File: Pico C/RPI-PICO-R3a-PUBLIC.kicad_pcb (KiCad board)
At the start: 2 copper layers, 53.7 x 21 mm, 53 parts, among them IC1 W25Q16JVUXIQ, J1 CON_PICO_40W_VER_C, J2 USB_C_Receptacle_USB2.0_16P, J3 SM03B-SRSS-TB, Q1 DMG1012T-7, U1 RP2040, U2 RT6150B-33GQW, Y1 ECS-120-8-33-JGN-TR

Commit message: Add files via upload
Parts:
- moved C16 0.71 mm to (135.0, 95.0)
- moved C17 0.28 mm to (136.2, 100.0)

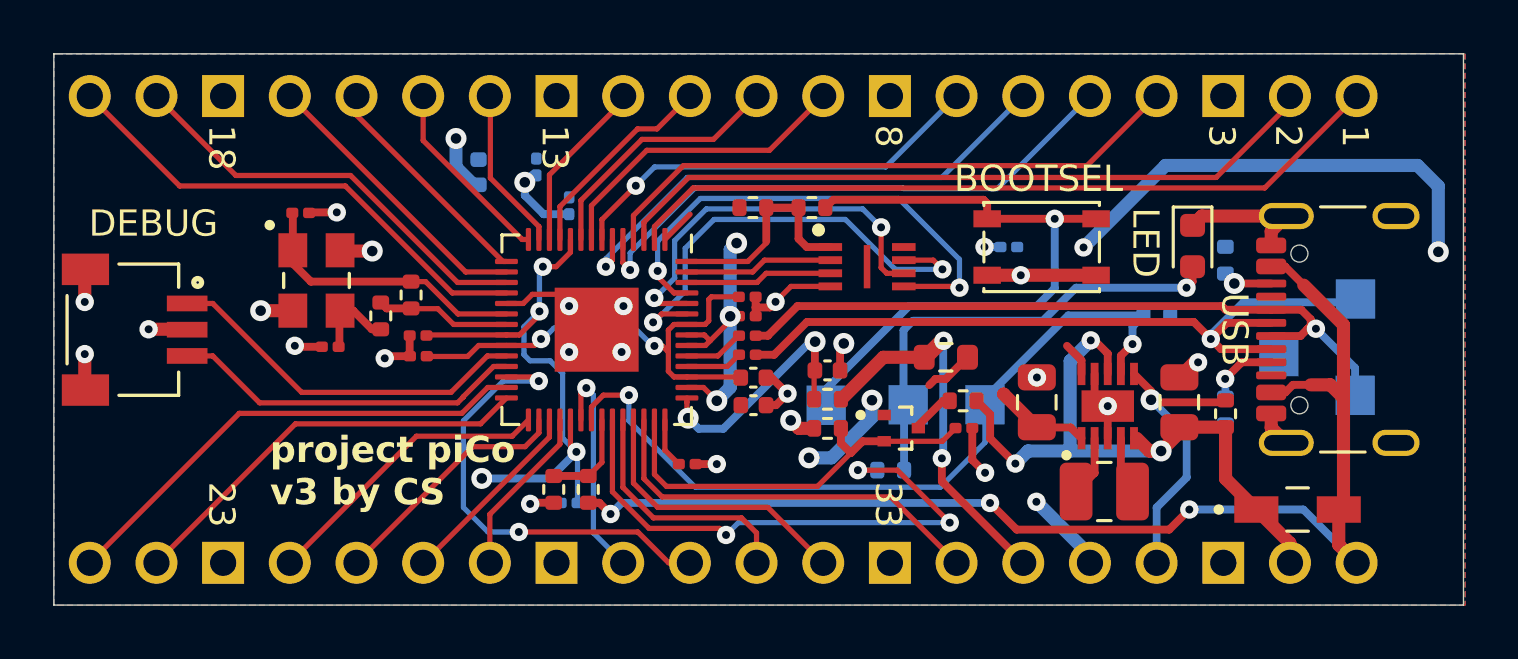
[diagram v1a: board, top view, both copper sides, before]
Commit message: Add files via upload
Upload boardview file for use with OpenBoardView.
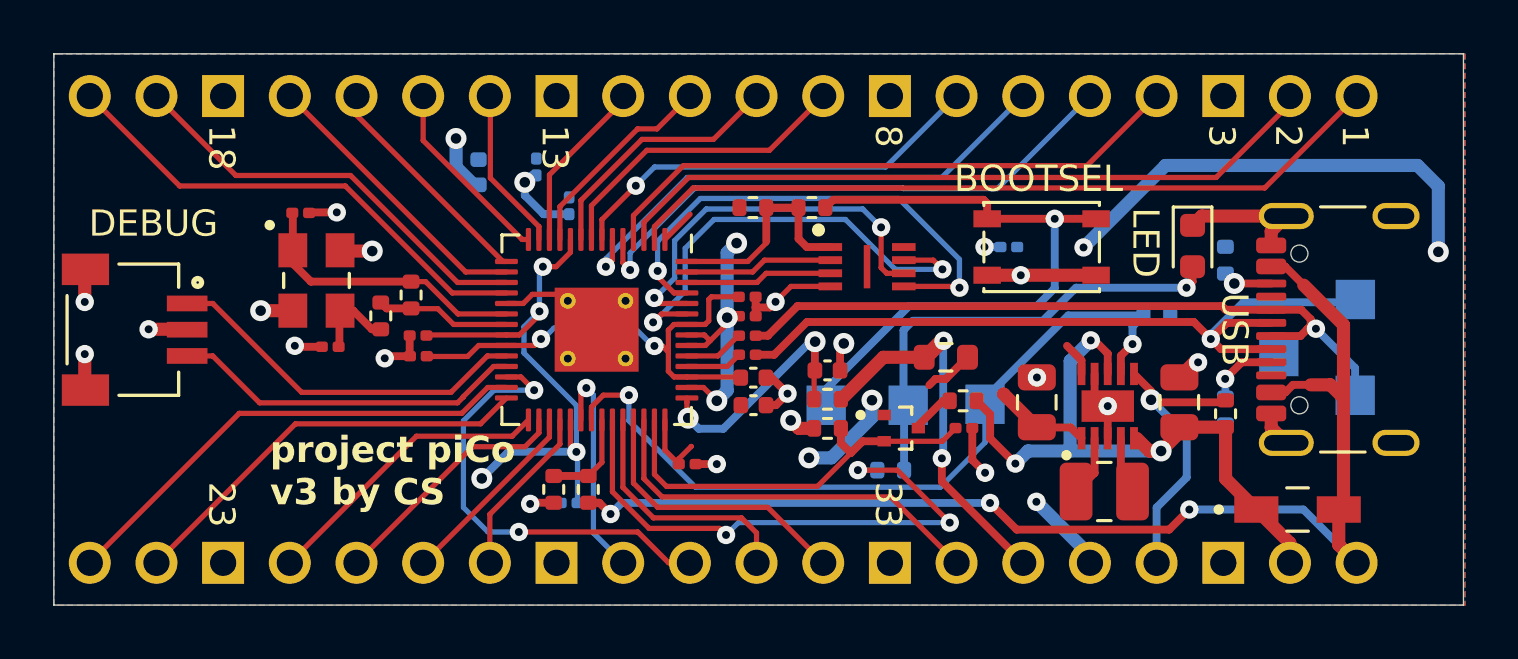
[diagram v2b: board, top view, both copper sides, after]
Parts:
- C10, C11, C15, C16, C17, C3, C4, C5, C6, C7, C8, C9: footprint Capacitor_SMD:C_0201_0603Metric -> Pico_C:C_0201_0603Metric
- R14, R15: footprint Resistor_SMD:R_0201_0603Metric -> Pico_C:R_0201_0603Metric
- U1: footprint Pico_C:QFN-56-1EP_7x7mm_P0.4mm_EP3.2x3.2mm -> Pico_C:QFN-56-1EP_7x7mm_P0.4mm_EP3.2x3.2mm_ThermalVias
- turned C3 to 0 degrees
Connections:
- C3 pad 1: GND -> GPIO29_ADC3
- C3 pad 2: GPIO29_ADC3 -> GND
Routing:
- net GND: track 39.2 -> 40.8 mm, vias 23 -> 19

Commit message: Add files via upload
Changed VSS to VS to reflect that it is a system voltage and not a negative supply/GND.
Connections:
- net VSS renamed VS
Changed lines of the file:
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@@
   (net 0 "")
   (net 1 "+3V3")
-  (net 2 "VSS")
+  (net 2 "VS")
   (net 3 "VBUS")
   (net 4 "Net-(U2-LX1)")
@@
       (net 16 "Net-(Q1-D)") (pintype "passive"))
     (pad "2" smd roundrect (at 0.51 0) (size 0.54 0.64) (layers "F.Cu" "F.Paste" "F.Mask") (roundrect_rratio 0.25)
-      (net 2 "VSS") (pintype "passive"))
+      (net 2 "VS") (pintype "passive"))
     (model "${KICAD6_3DMODEL_DIR}/Resistor_SMD.3dshapes/R_0402_1005Metric.wrl"
       (offset (xyz 0 0 0))
@@
       (stroke (width 0.2) (type solid)) (fill none) (layer "F.Fab"))
     (pad "1" smd rect (at -1.57 0) (size 1.68 1.01) (layers "F.Cu" "F.Paste" "F.Mask")
-      (net 2 "VSS") (pintype "unspecified") (solder_mask_margin 0.102))
+      (net 2 "VS") (pintype "unspecified") (solder_mask_margin 0.102))
     (pad "2" smd rect (at 1.57 0) (size 1.68 1.01) (layers "F.Cu" "F.Paste" "F.Mask")
       (net 3 "VBUS") (pintype "unspecified") (solder_mask_margin 0.102))
@@
       (net 58 "GND") (pintype "input"))
     (pad "39" thru_hole circle (at 8.89 -21.59 270) (size 1.6 1.6) (drill 1) (layers "*.Cu" "*.Mask")
-      (net 2 "VSS") (pintype "input"))
+      (net 2 "VS") (pintype "input"))
     (pad "40" thru_hole circle (at 8.89 -24.13 270) (size 1.6 1.6) (drill 1) (layers "*.Cu" "*.Mask")
       (net 3 "VBUS") (pintype "input"))
@@
       (net 13 "/3V3_EN") (pintype "passive"))
     (pad "2" smd roundrect (at 0.51 0 270) (size 0.54 0.64) (layers "F.Cu" "F.Paste" "F.Mask") (roundrect_rratio 0.25)
-      (net 2 "VSS") (pintype "passive"))
+      (net 2 "VS") (pintype "passive"))
     (model "${KICAD6_3DMODEL_DIR}/Resistor_SMD.3dshapes/R_0402_1005Metric.wrl"
       (offset (xyz 0 0 0))
@@
       (net 4 "Net-(U2-LX1)") (pinfunction "LX1") (pintype "passive"))
     (pad "5" smd rect (at -1.225 1 90) (size 0.85 0.3) (layers "F.Cu" "F.Paste")
-      (net 2 "VSS") (pinfunction "VIN") (pintype "input"))
+      (net 2 "VS") (pinfunction "VIN") (pintype "input"))
     (pad "6" smd rect (at 1.225 1 90) (size 0.85 0.3) (layers "F.Cu" "F.Paste")
       (net 13 "/3V3_EN") (pinfunction "EN") (pintype "input"))
@@
       (net 61 "GPIO23") (pinfunction "PS") (pintype "input"))
     (pad "8" smd rect (at 1.225 0 90) (size 0.85 0.3) (layers "F.Cu" "F.Paste")
-      (net 2 "VSS") (pinfunction "VINA") (pintype "input"))
+      (net 2 "VS") (pinfunction "VINA") (pintype "input"))
     (pad "9" smd rect (at 1.225 -0.5 90) (size 0.85 0.3) (layers "F.Cu" "F.Paste")
       (net 58 "GND") (pinfunction "GND") (pintype "power_in"))
@@
       (stroke (width 0.1) (type solid)) (layer "F.Fab"))
     (pad "1" smd roundrect (at -0.95 0 90) (size 1 1.45) (layers "F.Cu" "F.Paste" "F.Mask") (roundrect_rratio 0.25)
-      (net 2 "VSS") (pintype "passive"))
+      (net 2 "VS") (pintype "passive"))
     (pad "2" smd roundrect (at 0.95 0 90) (size 1 1.45) (layers "F.Cu" "F.Paste" "F.Mask") (roundrect_rratio 0.25)
       (net 58 "GND") (pintype "passive"))

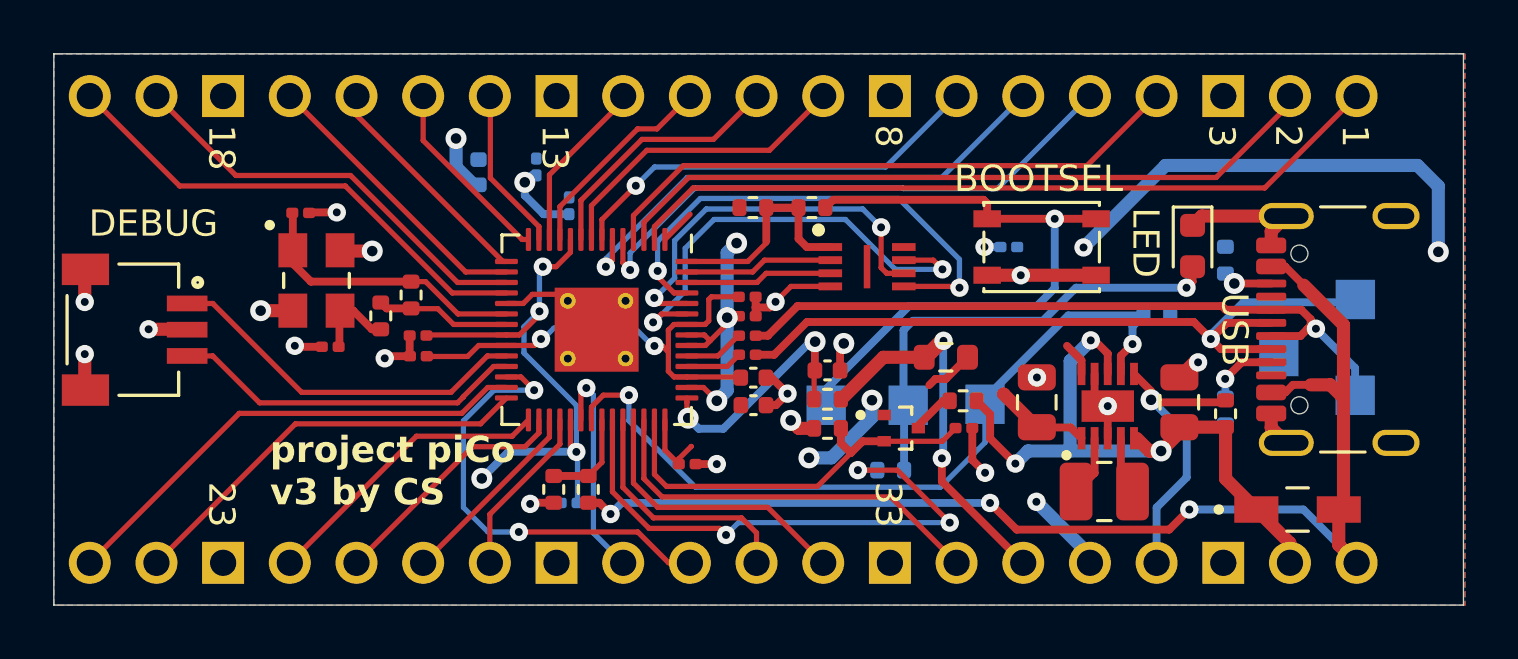
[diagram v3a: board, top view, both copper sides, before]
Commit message: Add files via upload
Updated design and included official design file from the Pi Foundation.
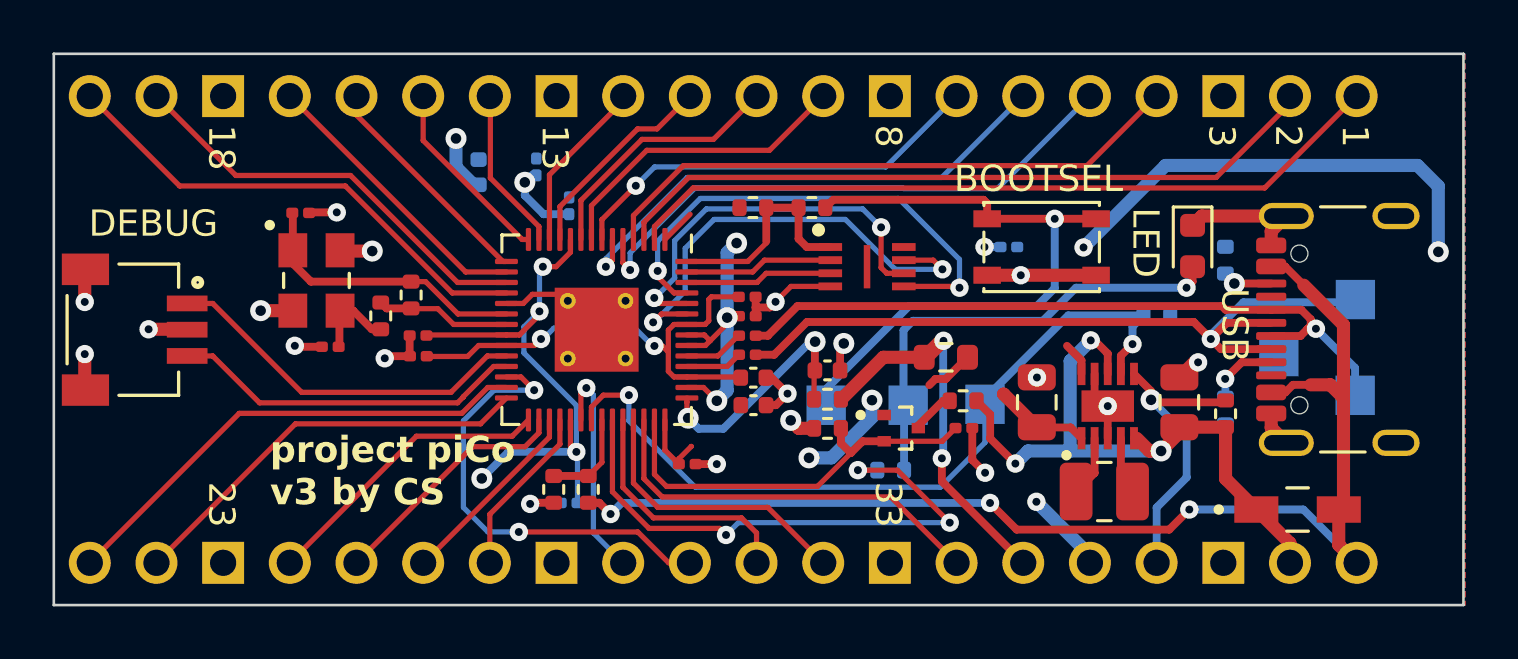
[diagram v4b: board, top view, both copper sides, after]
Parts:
- added J4: SM03B-SRSS-TB, Pico_C:JST_SM03B-SRSS-TB_LF__SN_, F.Cu at (130.7, 99.4)
- J1: value CON_PICO_40W_VER_C -> ~; footprint Pico_C:CON_PICO_40W_VER_C -> Pico_C:CON_PICO_1-20
- J2: value USB_C_Receptacle_USB2.0_16P -> ~; footprint Connector_USB:USB_C_Receptacle_GCT_USB4105-xx-A_16P_TopMnt_Horizontal -> Pico_C:CON_PICO_21-40
- J3: value SM03B-SRSS-TB -> USB_C_Receptacle_USB2.0_16P; footprint Pico_C:JST_SM03B-SRSS-TB_LF__SN_ -> Connector_USB:USB_C_Receptacle_GCT_USB4105-xx-A_16P_TopMnt_Horizontal
- moved J3 45.0 mm to (175.7, 99.4), turned to 90 degrees
- moved J2 24.6 mm to (151.1, 99.4), turned to -90 degrees
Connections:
- R1 pad 1: Net-(J2-CC1) -> Net-(J3-CC1)
- R2 pad 1: Net-(J2-CC2) -> Net-(J3-CC2)
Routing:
- net Net-(J3-CC1): track 0.00 -> 2.74 mm, vias 0 -> 1
- net Net-(J2-CC1): track 2.74 -> 0.00 mm, vias 1 -> 0
- net Net-(J3-CC2): track 0.00 -> 1.93 mm, vias 0 -> 1
- net Net-(J2-CC2): track 1.93 -> 0.00 mm, vias 1 -> 0
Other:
- board text added: "USB"
